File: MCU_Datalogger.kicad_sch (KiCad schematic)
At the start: 25 parts, among them U1 DS1337S_, U2 24LC1025, U3 24LC1025, U4 ATMEGA328P-AU, Y1 32.768 KHz, Y2 16 MHz

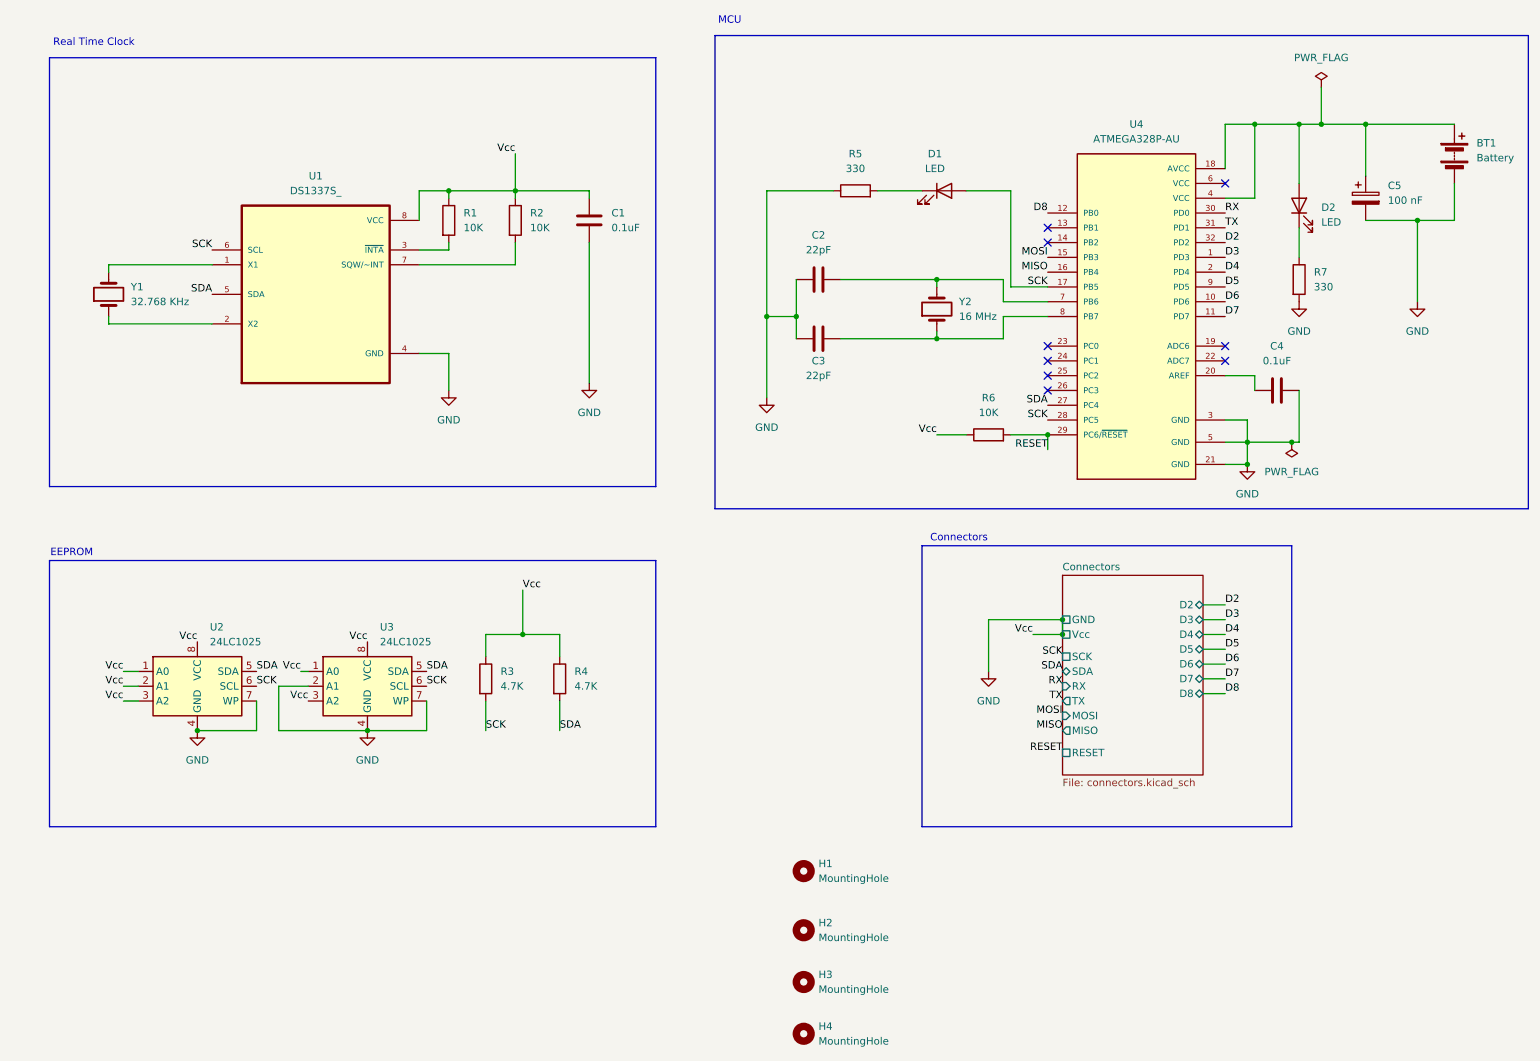
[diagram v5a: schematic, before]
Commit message: Problem in 9 pin connector
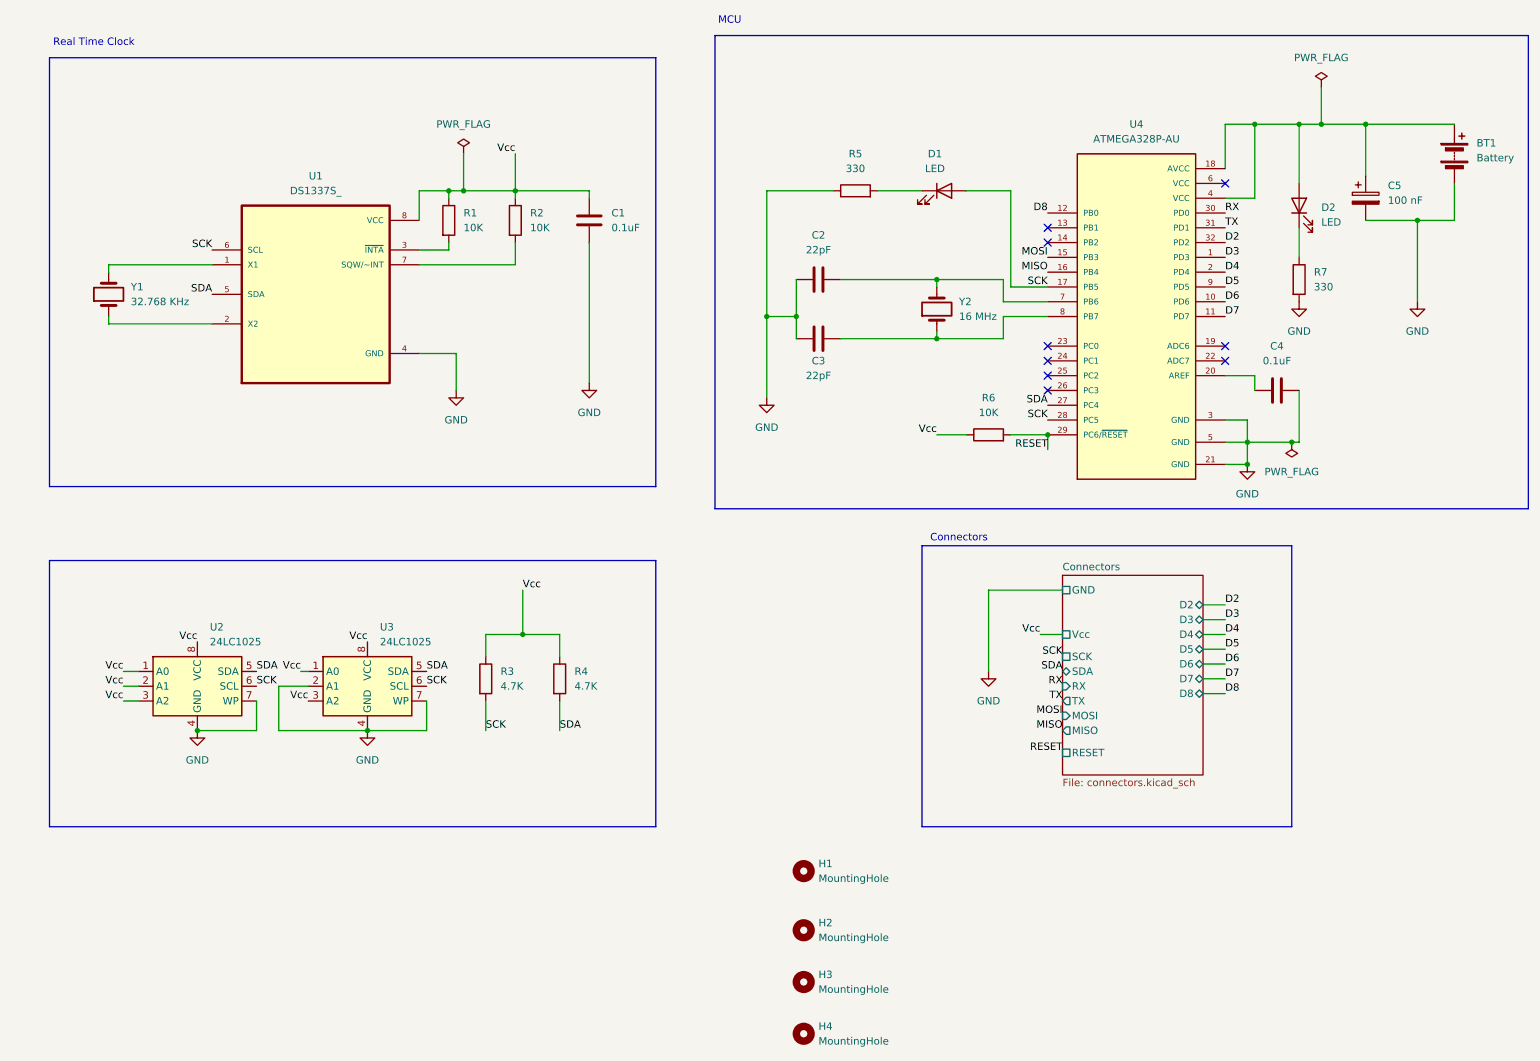
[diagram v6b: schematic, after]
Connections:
- net GND: no longer C1.1, R1.1, R2.1, R3.1, R4.1, R6.1, U1.8 (VCC), U2.1 (A0), U2.2 (A1), U2.3 (A2), U2.8 (VCC), U3.1 (A0), U3.3 (A2), U3.8 (VCC)
- new net Vcc: C1.1, R1.1, R2.1, R3.1, R4.1, R6.1, U1.8 (VCC), U2.1 (A0), U2.2 (A1), U2.3 (A2), U2.8 (VCC), U3.1 (A0), U3.3 (A2), U3.8 (VCC)
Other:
- note removed: "EEPROM"
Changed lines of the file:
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@@
 		)
 	)
-	(text "EEPROM"
-		(exclude_from_sim no)
-		(at 33.02 106.68 0)
-		(effects
-			(font
-				(size 1.27 1.27)
-			)
-		)
-	)
 	(text "MCU\n"
 		(exclude_from_sim no)
@@
 	)
 	(junction
-		(at 109.22 44.45)
+		(at 100.33 44.45)
 		(diameter 0)
 		(color 0 0 0 0)
 	)
 	(junction
-		(at 247.65 33.02)
+		(at 109.22 44.45)
 		(diameter 0)
 		(color 0 0 0 0)
 	)
 	(junction
-		(at 203.2 120.65)
+		(at 247.65 33.02)
 		(diameter 0)
 		(color 0 0 0 0)
@@
 	)
 	(junction
-		(at 203.2 118.11)
-		(diameter 0)
-		(color 0 0 0 0)
-	)
-	(junction
 		(at 157.48 66.04)
 		(diameter 0)
@@
 	(wire
 		(pts
-			(xy 92.71 72.39) (xy 97.79 72.39)
+			(xy 109.22 38.1) (xy 109.22 44.45)
 		)
 		(stroke
@@
 	(wire
 		(pts
-			(xy 109.22 38.1) (xy 109.22 44.45)
+			(xy 64.77 137.16) (xy 54.61 137.16)
 		)
 		(stroke
@@
 	(wire
 		(pts
-			(xy 64.77 137.16) (xy 54.61 137.16)
+			(xy 41.91 127) (xy 44.45 127)
 		)
 		(stroke
@@
 	(wire
 		(pts
-			(xy 190.5 118.11) (xy 203.2 118.11)
+			(xy 97.79 54.61) (xy 97.79 53.34)
 		)
 		(stroke
@@
 	(wire
 		(pts
-			(xy 41.91 127) (xy 44.45 127)
+			(xy 68.58 129.54) (xy 68.58 137.16)
 		)
 		(stroke
@@
 	(wire
 		(pts
-			(xy 97.79 54.61) (xy 97.79 53.34)
+			(xy 231.14 45.72) (xy 236.22 45.72)
 		)
 		(stroke
@@
 	(wire
 		(pts
-			(xy 68.58 129.54) (xy 68.58 137.16)
+			(xy 57.15 67.31) (xy 39.37 67.31)
 		)
 		(stroke
@@
 	(wire
 		(pts
-			(xy 231.14 45.72) (xy 236.22 45.72)
+			(xy 39.37 58.42) (xy 39.37 57.15)
 		)
 		(stroke
@@
 	(wire
 		(pts
-			(xy 57.15 67.31) (xy 39.37 67.31)
+			(xy 181.61 86.36) (xy 186.69 86.36)
 		)
 		(stroke
@@
 	(wire
 		(pts
-			(xy 39.37 58.42) (xy 39.37 57.15)
+			(xy 255.27 33.02) (xy 270.51 33.02)
 		)
 		(stroke
@@
 	(wire
 		(pts
-			(xy 181.61 86.36) (xy 186.69 86.36)
+			(xy 157.48 66.04) (xy 157.48 69.85)
 		)
 		(stroke
@@
 	(wire
 		(pts
-			(xy 255.27 33.02) (xy 270.51 33.02)
+			(xy 193.04 66.04) (xy 193.04 69.85)
 		)
 		(stroke
@@
 	(wire
 		(pts
-			(xy 157.48 66.04) (xy 157.48 69.85)
+			(xy 41.91 132.08) (xy 44.45 132.08)
 		)
 		(stroke
@@
 	(wire
 		(pts
-			(xy 193.04 66.04) (xy 193.04 69.85)
+			(xy 109.22 44.45) (xy 109.22 45.72)
 		)
 		(stroke
@@
 	(wire
 		(pts
-			(xy 109.22 44.45) (xy 109.22 45.72)
+			(xy 109.22 57.15) (xy 109.22 53.34)
 		)
 		(stroke
@@
 	(wire
 		(pts
-			(xy 109.22 57.15) (xy 109.22 53.34)
+			(xy 97.79 44.45) (xy 100.33 44.45)
 		)
 		(stroke
@@
 	(wire
 		(pts
-			(xy 97.79 44.45) (xy 109.22 44.45)
+			(xy 190.5 113.03) (xy 203.2 113.03)
 		)
 		(stroke
@@
 	(wire
 		(pts
-			(xy 97.79 72.39) (xy 97.79 78.74)
+			(xy 99.06 72.39) (xy 99.06 78.74)
 		)
 		(stroke
@@
 	(wire
 		(pts
-			(xy 41.91 132.08) (xy 44.45 132.08)
+			(xy 100.33 44.45) (xy 109.22 44.45)
 		)
 		(stroke
@@
 	(wire
 		(pts
+			(xy 100.33 38.1) (xy 100.33 44.45)
+		)
+		(stroke
+			(width 0)
+			(type default)
+		)
+	)
+	(wire
+		(pts
 			(xy 227.33 118.11) (xy 231.14 118.11)
 		)
@@
 	(wire
 		(pts
-			(xy 41.91 129.54) (xy 44.45 129.54)
-		)
-		(stroke
-			(width 0)
-			(type default)
-		)
-	)
-	(wire
-		(pts
 			(xy 200.66 88.9) (xy 200.66 86.36)
 		)
@@
 	(wire
 		(pts
-			(xy 203.2 118.11) (xy 203.2 120.65)
+			(xy 181.61 69.85) (xy 181.61 68.58)
 		)
 		(stroke
@@
 	(wire
 		(pts
-			(xy 181.61 69.85) (xy 181.61 68.58)
+			(xy 193.04 69.85) (xy 181.61 69.85)
 		)
 		(stroke
@@
 	(wire
 		(pts
-			(xy 193.04 69.85) (xy 181.61 69.85)
+			(xy 199.39 120.65) (xy 203.2 120.65)
 		)
 		(stroke
@@
 	(wire
 		(pts
+			(xy 92.71 72.39) (xy 99.06 72.39)
+		)
+		(stroke
+			(width 0)
+			(type default)
+		)
+	)
+	(wire
+		(pts
 			(xy 236.22 45.72) (xy 236.22 33.02)
 		)
@@
 	(wire
 		(pts
+			(xy 41.91 129.54) (xy 44.45 129.54)
+		)
+		(stroke
+			(width 0)
+			(type default)
+		)
+	)
+	(wire
+		(pts
 			(xy 110.49 120.65) (xy 110.49 113.03)
 		)
@@
 	(wire
 		(pts
-			(xy 190.5 118.11) (xy 190.5 127)
+			(xy 190.5 113.03) (xy 190.5 127)
 		)
 		(stroke
@@
 	(wire
 		(pts
-			(xy 198.12 120.65) (xy 203.2 120.65)
-		)
-		(stroke
-			(width 0)
-			(type default)
-		)
-	)
-	(wire
-		(pts
 			(xy 255.27 49.53) (xy 264.16 49.53)
 		)
@@
 		)
 	)
-	(label "Vcc"
-		(at 41.91 132.08 180)
-		(effects
-			(font
-				(size 1.27 1.27)
-			)
-			(justify right bottom)
-		)
-	)
 	(label "D8"
 		(at 200.66 48.26 180)
@@
 		)
 	)
+	(label "Vcc"
+		(at 199.39 120.65 180)
+		(effects
+			(font
+				(size 1.27 1.27)
+			)
+			(justify right bottom)
+		)
+	)
 	(label "SCK"
 		(at 57.15 54.61 180)
@@
 		)
 	)
-	(label "Vcc"
-		(at 198.12 120.65 180)
-		(effects
-			(font
-				(size 1.27 1.27)
-			)
-			(justify right bottom)
-		)
-	)
 	(label "MISO"
 		(at 200.66 58.42 180)
@@
 	)
 	(label "Vcc"
+		(at 41.91 132.08 180)
+		(effects
+			(font
+				(size 1.27 1.27)
+			)
+			(justify right bottom)
+		)
+	)
+	(label "Vcc"
 		(at 110.49 113.03 0)
 		(effects
@@
 	(symbol
 		(lib_id "power:GND")
-		(at 97.79 78.74 0)
+		(at 99.06 78.74 0)
 		(unit 1)
 		(exclude_from_sim no)
@@
 		(fields_autoplaced yes)
 		(property "Reference" "#PWR01"
-			(at 97.79 85.09 0)
+			(at 99.06 85.09 0)
 			(effects
 				(font
@@
 		)
 		(property "Value" "GND"
-			(at 97.79 83.82 0)
+			(at 99.06 83.82 0)
 			(effects
 				(font
@@
 		)
 		(property "Footprint" ""
-			(at 97.79 78.74 0)
+			(at 99.06 78.74 0)
 			(effects
 				(font
@@
 		)
 		(property "Datasheet" ""
-			(at 97.79 78.74 0)
+			(at 99.06 78.74 0)
 			(effects
 				(font
@@
 		)
 		(property "Description" "Power symbol creates a global label with name \"GND\" , ground"
-			(at 97.79 78.74 0)
+			(at 99.06 78.74 0)
 			(effects
 				(font
@@
 	)
 	(symbol
+		(lib_id "power:PWR_FLAG")
+		(at 100.33 38.1 0)
+		(unit 1)
+		(exclude_from_sim no)
+		(in_bom yes)
+		(on_board yes)
+		(dnp no)
+		(fields_autoplaced yes)
+		(property "Reference" "#FLG03"
+			(at 100.33 36.195 0)
+			(effects
+				(font
+					(size 1.27 1.27)
+				)
+				(hide yes)
+			)
+		)
+		(property "Value" "PWR_FLAG"
+			(at 100.33 33.02 0)
+			(effects
+				(font
+					(size 1.27 1.27)
+				)
+			)
+		)
+		(property "Footprint" ""
+			(at 100.33 38.1 0)
+			(effects
+				(font
+					(size 1.27 1.27)
+				)
+				(hide yes)
+			)
+		)
+		(property "Datasheet" "~"
+			(at 100.33 38.1 0)
+			(effects
+				(font
+					(size 1.27 1.27)
+				)
+				(hide yes)
+			)
+		)
+		(property "Description" "Special symbol for telling ERC where power comes from"
+			(at 100.33 38.1 0)
+			(effects
+				(font
+					(size 1.27 1.27)
+				)
+				(hide yes)
+			)
+		)
+		(pin "1"
+		)
+		(instances
+			(project "MCU_Datalogger"
+				(path "/9a58bdc0-cf43-4f46-bdf9-3019f1d018de"
+					(reference "#FLG03")
+					(unit 1)
+				)
+			)
+		)
+	)
+	(symbol
 		(lib_id "power:GND")
 		(at 243.84 63.5 0)
@@
 			)
 		)
-		(pin "Vcc" passive
-			(at 203.2 120.65 180)
+		(pin "GND" passive
+			(at 203.2 113.03 180)
 			(effects
 				(font
@@
 			)
 		)
-		(pin "GND" passive
-			(at 203.2 118.11 180)
+		(pin "RX" input
+			(at 203.2 129.54 180)
 			(effects
 				(font
@@
 			)
 		)
-		(pin "RX" input
-			(at 203.2 129.54 180)
+		(pin "TX" output
+			(at 203.2 132.08 180)
 			(effects
 				(font
@@
 			)
 		)
-		(pin "TX" output
-			(at 203.2 132.08 180)
+		(pin "Vcc" passive
+			(at 203.2 120.65 180)
 			(effects
 				(font
